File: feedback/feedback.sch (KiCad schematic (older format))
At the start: 26 parts, among them J1 12V, J2 C, J3 AVR-ISP-6, J4 CAN, U1 ATmega32M1-AU, U2 LM317_SOT-223, U3 MCP2551-I-SN, Y1 16MHz

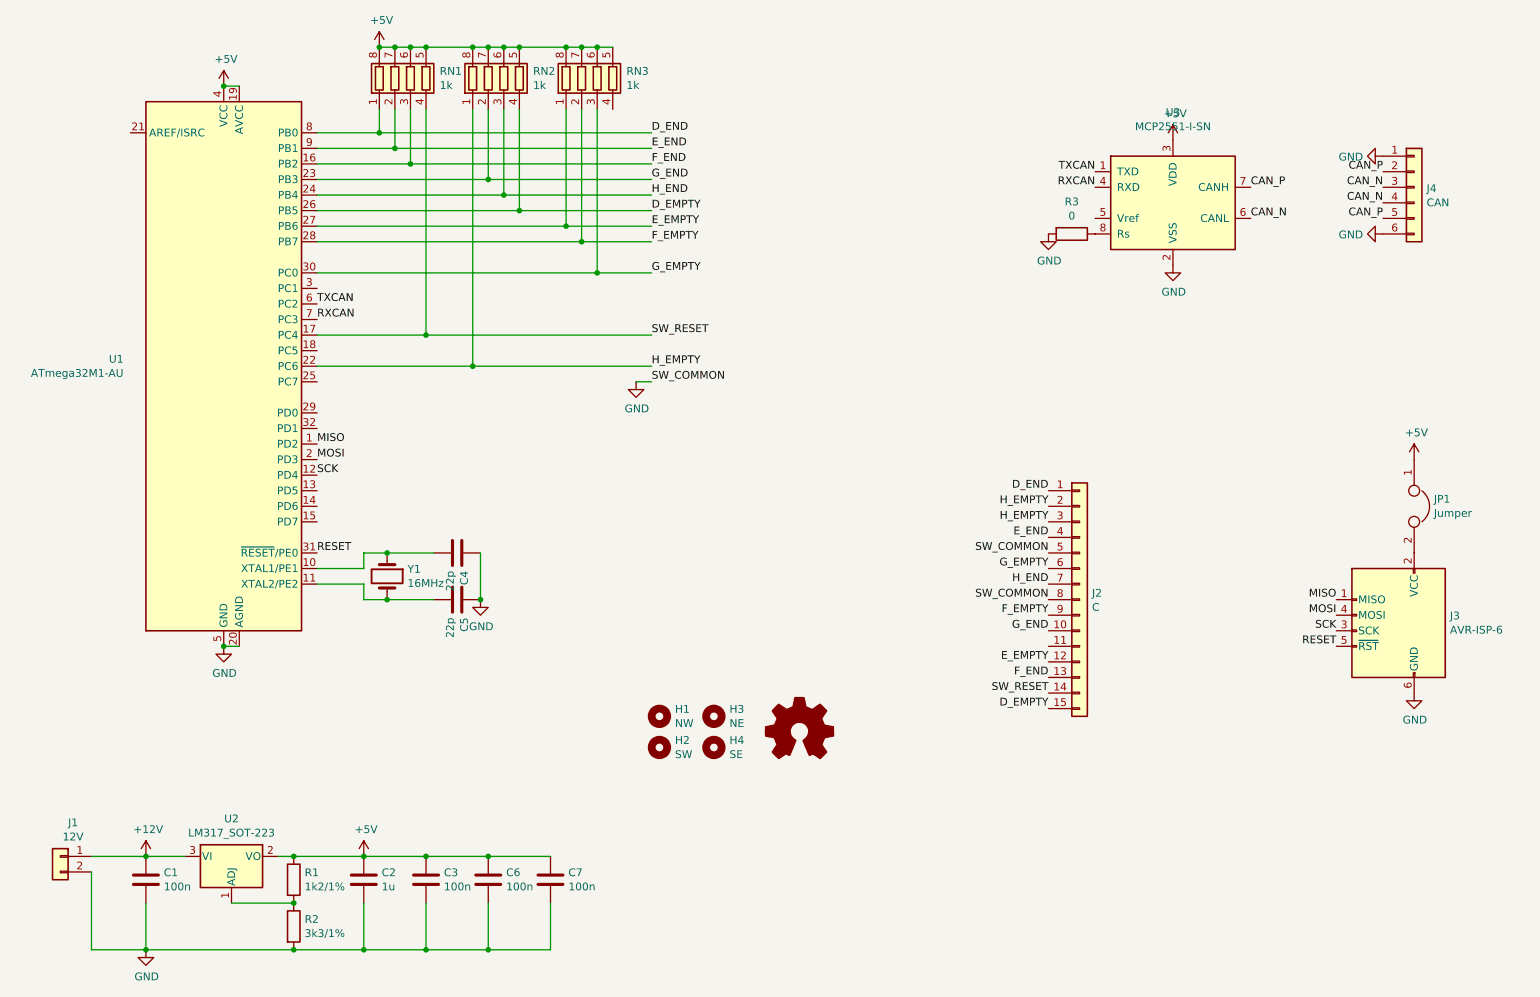
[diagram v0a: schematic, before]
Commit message: feedback: added separate terminal header
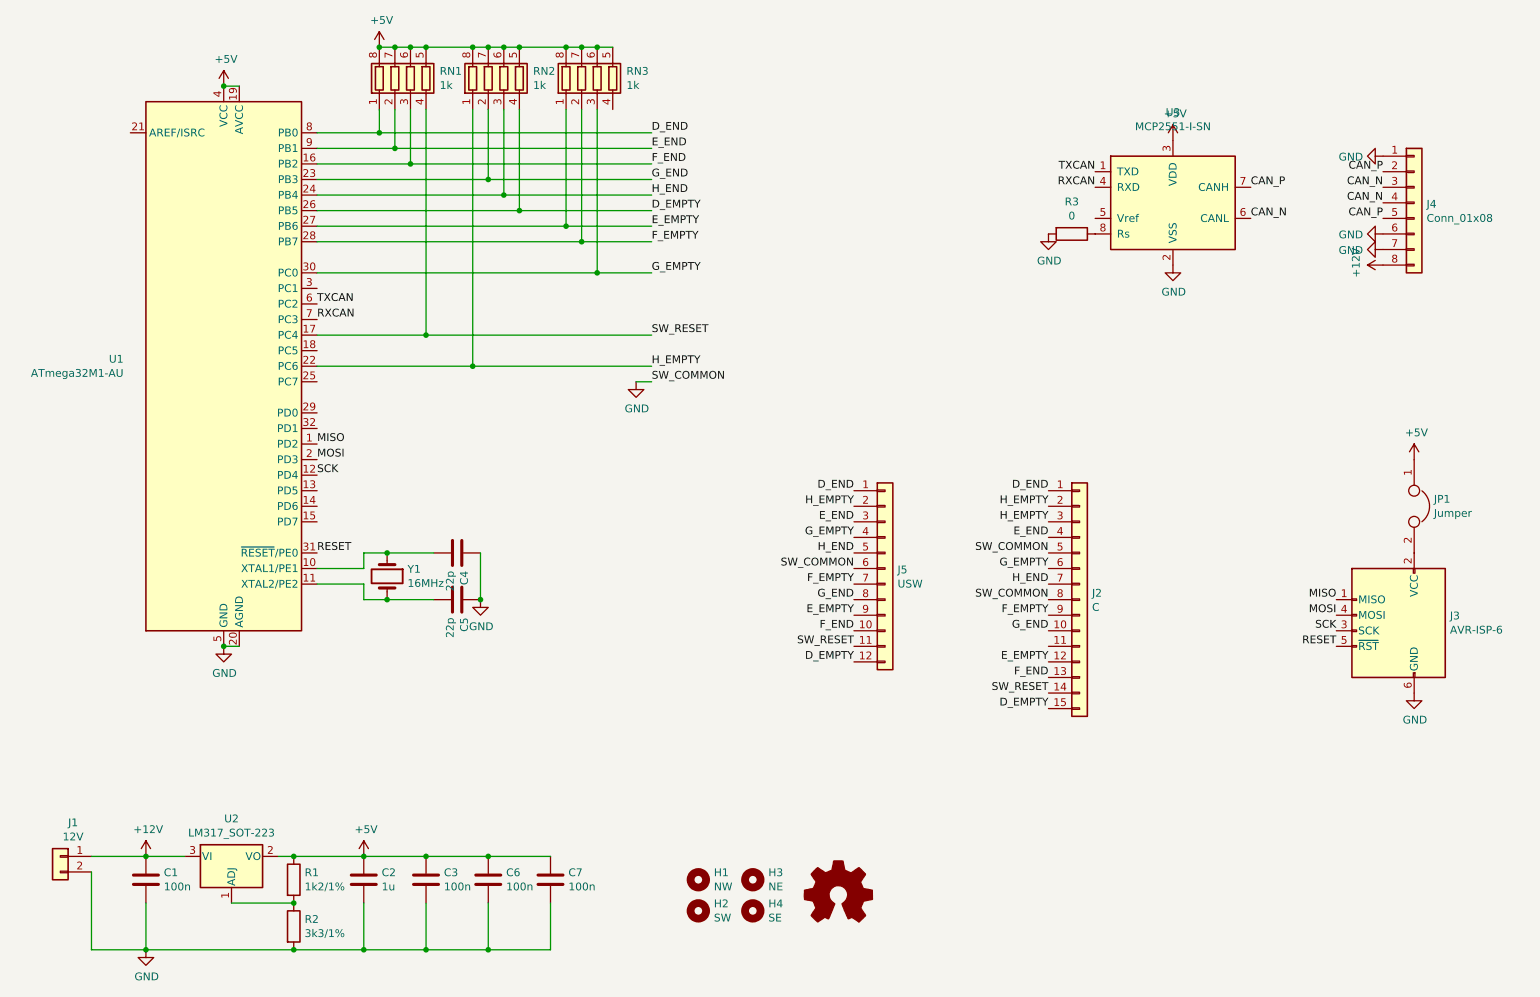
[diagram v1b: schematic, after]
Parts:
- removed J4: CAN, TerminalBlock_TE-Connectivity:TerminalBlock_TE_282834-6_1x06_P2.54mm_Horizontal, symbol Connector_Generic:Conn_01x06
- added J4: Conn_01x08, TerminalBlock_TE-Connectivity:TerminalBlock_TE_282834-8_1x08_P2.54mm_Horizontal, symbol Connector_Generic:Conn_01x08
- added J5: USW, TerminalBlock_TE-Connectivity:TerminalBlock_TE_1-282834-2_1x12_P2.54mm_Horizontal, symbol Connector_Generic:Conn_01x12
- added OHW1: Logo_Open_Hardware_Small, Symbol:OSHW-Logo2_7.3x6mm_SilkScreen, symbol Graphic:Logo_Open_Hardware_Small
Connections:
- net +12V: now also J4.8 (Pin_8)
- net CAN_N: now also J4.3 (Pin_3), J4.4 (Pin_4)
- net CAN_P: now also J4.2 (Pin_2), J4.5 (Pin_5)
- net D_EMPTY: now also J5.12 (Pin_12)
- net D_END: now also J5.1 (Pin_1)
- net E_EMPTY: now also J5.9 (Pin_9)
- net E_END: now also J5.3 (Pin_3)
- net F_EMPTY: now also J5.7 (Pin_7)
- net F_END: now also J5.10 (Pin_10)
- net GND: now also J4.1 (Pin_1), J4.6 (Pin_6), J4.7 (Pin_7), J5.6 (Pin_6)
- net G_EMPTY: now also J5.4 (Pin_4)
- net G_END: now also J5.8 (Pin_8)
- net H_EMPTY: now also J5.2 (Pin_2)
- net H_END: now also J5.5 (Pin_5)
- net SW_RESET: now also J5.11 (Pin_11)
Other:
- moved on the sheet: H1, H2, H3, H4
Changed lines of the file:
@@
 	3550 4950 3850 4950
-$Comp
-L Connector_Generic:Conn_01x06 J4
-U 1 1 5F42D3E5
-P 10150 2300
-F 0 "J4" H 10230 2292 50  0000 L CNN
-F 1 "CAN" H 10230 2201 50  0000 L CNN
-F 2 "TerminalBlock_TE-Connectivity:TerminalBlock_TE_282834-6_1x06_P2.54mm_Horizontal" H 10150 2300 50  0001 C CNN
-F 3 "~" H 10150 2300 50  0001 C CNN
-	1    10150 2300
-	1    0    0    -1
-$EndComp
 $Comp
 L Device:C C7
@@
 L Mechanical:MountingHole H1
 U 1 1 5F4AAF51
-P 5300 5700
-F 0 "H1" H 5400 5746 50  0000 L CNN
-F 1 "NW" H 5400 5655 50  0000 L CNN
-F 2 "MountingHole:MountingHole_3.2mm_M3_ISO7380" H 5300 5700 50  0001 C CNN
-F 3 "~" H 5300 5700 50  0001 C CNN
-	1    5300 5700
+P 5550 6750
+F 0 "H1" H 5650 6796 50  0000 L CNN
+F 1 "NW" H 5650 6705 50  0000 L CNN
+F 2 "MountingHole:MountingHole_3.2mm_M3_ISO7380" H 5550 6750 50  0001 C CNN
+F 3 "~" H 5550 6750 50  0001 C CNN
+	1    5550 6750
 	1    0    0    -1
 $EndComp
@@
 L Mechanical:MountingHole H3
 U 1 1 5F4AB624
-P 5650 5700
-F 0 "H3" H 5750 5746 50  0000 L CNN
-F 1 "NE" H 5750 5655 50  0000 L CNN
-F 2 "MountingHole:MountingHole_3.2mm_M3_ISO7380" H 5650 5700 50  0001 C CNN
-F 3 "~" H 5650 5700 50  0001 C CNN
-	1    5650 5700
+P 5900 6750
+F 0 "H3" H 6000 6796 50  0000 L CNN
+F 1 "NE" H 6000 6705 50  0000 L CNN
+F 2 "MountingHole:MountingHole_3.2mm_M3_ISO7380" H 5900 6750 50  0001 C CNN
+F 3 "~" H 5900 6750 50  0001 C CNN
+	1    5900 6750
 	1    0    0    -1
 $EndComp
@@
 L Mechanical:MountingHole H2
 U 1 1 5F4AB8DD
-P 5300 5900
-F 0 "H2" H 5400 5946 50  0000 L CNN
-F 1 "SW" H 5400 5855 50  0000 L CNN
-F 2 "MountingHole:MountingHole_3.2mm_M3_ISO7380" H 5300 5900 50  0001 C CNN
-F 3 "~" H 5300 5900 50  0001 C CNN
-	1    5300 5900
+P 5550 6950
+F 0 "H2" H 5650 6996 50  0000 L CNN
+F 1 "SW" H 5650 6905 50  0000 L CNN
+F 2 "MountingHole:MountingHole_3.2mm_M3_ISO7380" H 5550 6950 50  0001 C CNN
+F 3 "~" H 5550 6950 50  0001 C CNN
+	1    5550 6950
 	1    0    0    -1
 $EndComp
@@
 L Mechanical:MountingHole H4
 U 1 1 5F4ABDBC
-P 5650 5900
-F 0 "H4" H 5750 5946 50  0000 L CNN
-F 1 "SE" H 5750 5855 50  0000 L CNN
-F 2 "MountingHole:MountingHole_3.2mm_M3_ISO7380" H 5650 5900 50  0001 C CNN
-F 3 "~" H 5650 5900 50  0001 C CNN
-	1    5650 5900
-	1    0    0    -1
-$EndComp
-$Comp
-L Graphic:Logo_Open_Hardware_Small #LOGO1
+P 5900 6950
+F 0 "H4" H 6000 6996 50  0000 L CNN
+F 1 "SE" H 6000 6905 50  0000 L CNN
+F 2 "MountingHole:MountingHole_3.2mm_M3_ISO7380" H 5900 6950 50  0001 C CNN
+F 3 "~" H 5900 6950 50  0001 C CNN
+	1    5900 6950
+	1    0    0    -1
+$EndComp
+$Comp
+L Graphic:Logo_Open_Hardware_Small OHW1
 U 1 1 5F4AC80D
-P 6200 5800
-F 0 "#LOGO1" H 6200 6075 50  0001 C CNN
-F 1 "Logo_Open_Hardware_Small" H 6200 5575 50  0001 C CNN
-F 2 "Symbol:OSHW-Logo2_7.3x6mm_SilkScreen" H 6200 5800 50  0001 C CNN
-F 3 "~" H 6200 5800 50  0001 C CNN
-	1    6200 5800
+P 6450 6850
+F 0 "OHW1" H 6450 7125 50  0001 C CNN
+F 1 "Logo_Open_Hardware_Small" H 6450 6625 50  0001 C CNN
+F 2 "Symbol:OSHW-Logo2_7.3x6mm_SilkScreen" H 6450 6850 50  0001 C CNN
+F 3 "~" H 6450 6850 50  0001 C CNN
+	1    6450 6850
 	1    0    0    -1
 $EndComp
@@
 Wire Wire Line
 	4900 2850 5250 2850
+$Comp
+L Connector_Generic:Conn_01x12 J5
+U 1 1 5F526155
+P 6750 4750
+F 0 "J5" H 6830 4742 50  0000 L CNN
+F 1 "USW" H 6830 4651 50  0000 L CNN
+F 2 "TerminalBlock_TE-Connectivity:TerminalBlock_TE_1-282834-2_1x12_P2.54mm_Horizontal" H 6750 4750 50  0001 C CNN
+F 3 "~" H 6750 4750 50  0001 C CNN
+	1    6750 4750
+	1    0    0    -1
+$EndComp
+Text Label 6550 4750 2    50   ~ 0
+SW_COMMON
+Text Label 6550 5250 2    50   ~ 0
+SW_RESET
+Text Label 6550 4250 2    50   ~ 0
+D_END
+Text Label 6550 4450 2    50   ~ 0
+E_END
+Text Label 6550 4650 2    50   ~ 0
+H_END
+Text Label 6550 4950 2    50   ~ 0
+G_END
+Text Label 6550 5150 2    50   ~ 0
+F_END
+Text Label 6550 4350 2    50   ~ 0
+H_EMPTY
+Text Label 6550 4550 2    50   ~ 0
+G_EMPTY
+Text Label 6550 4850 2    50   ~ 0
+F_EMPTY
+Text Label 6550 5050 2    50   ~ 0
+E_EMPTY
+Text Label 6550 5350 2    50   ~ 0
+D_EMPTY
+$Comp
+L Connector_Generic:Conn_01x08 J4
+U 1 1 5F52B034
+P 10150 2400
+F 0 "J4" H 10230 2392 50  0000 L CNN
+F 1 "Conn_01x08" H 10230 2301 50  0000 L CNN
+F 2 "TerminalBlock_TE-Connectivity:TerminalBlock_TE_282834-8_1x08_P2.54mm_Horizontal" H 10150 2400 50  0001 C CNN
+F 3 "~" H 10150 2400 50  0001 C CNN
+	1    10150 2400
+	1    0    0    -1
+$EndComp
+$Comp
+L power:GND #PWR0103
+U 1 1 5F52C53A
+P 9950 2700
+F 0 "#PWR0103" H 9950 2450 50  0001 C CNN
+F 1 "GND" V 9955 2572 50  0000 R CNN
+F 2 "" H 9950 2700 50  0001 C CNN
+F 3 "" H 9950 2700 50  0001 C CNN
+	1    9950 2700
+	0    1    1    0
+$EndComp
+$Comp
+L power:+12V #PWR0104
+U 1 1 5F52CA60
+P 9950 2800
+F 0 "#PWR0104" H 9950 2650 50  0001 C CNN
+F 1 "+12V" H 9965 2973 50  0000 C CNN
+F 2 "" H 9950 2800 50  0001 C CNN
+F 3 "" H 9950 2800 50  0001 C CNN
+	1    9950 2800
+	0    -1   -1   0
+$EndComp
 $EndSCHEMATC
